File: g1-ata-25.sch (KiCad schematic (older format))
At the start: 1 part

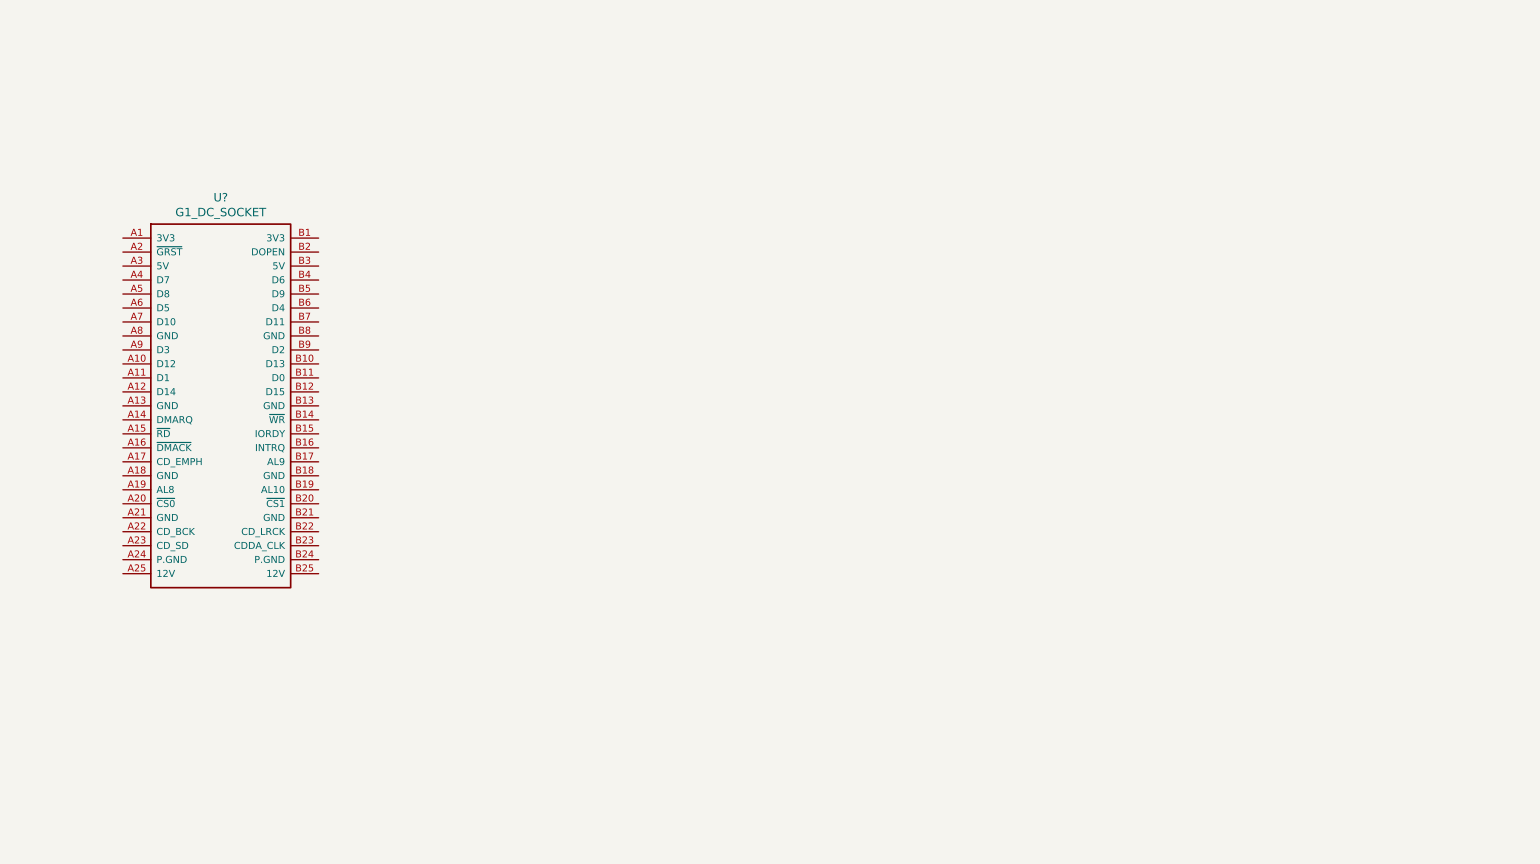
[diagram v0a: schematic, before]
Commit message: Added IDE connectors and enhanced g1-dc-socket numbering.
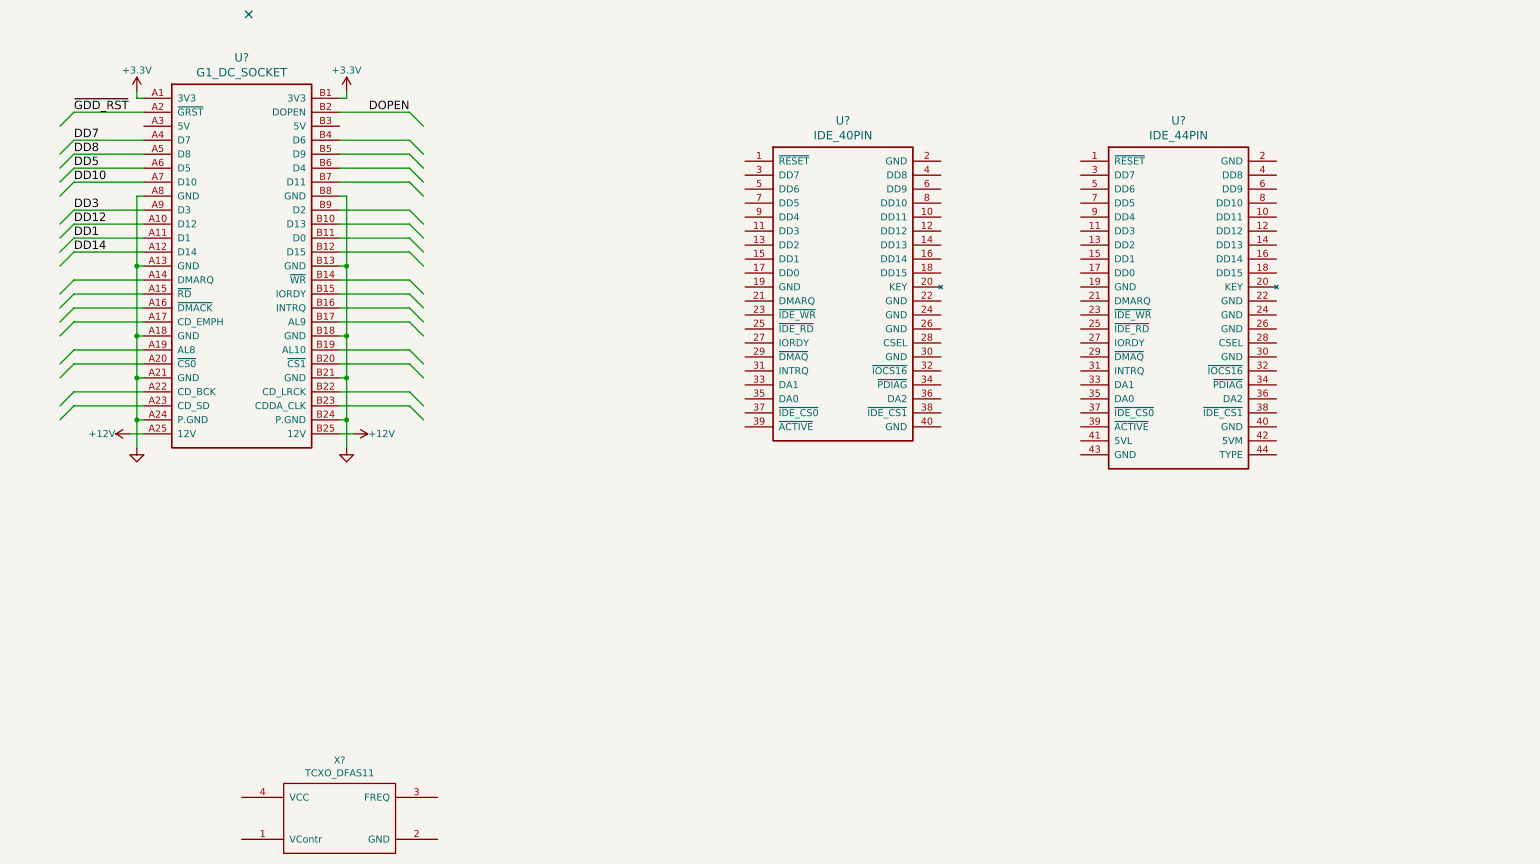
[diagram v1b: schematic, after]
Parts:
- added U?: IDE_40PIN, symbol IDE_40PIN
- added U?: IDE_44PIN, symbol IDE_44PIN
- added X?: TCXO_DFAS11, symbol TCXO_DFAS11
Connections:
- net +3V3: now reaches U?.A1 (3V3)
- net +3V3: now also U?.B1 (3V3)
- net DD12: now reaches U?.A10 (D12)
- net DD1: now reaches U?.A11 (D1)
- net DD14: now reaches U?.A12 (D14)
- net GND: now reaches U?.A13 (GND)
- net GND: now also U?.A18 (GND), U?.A21 (GND), U?.A24 (P.GND), U?.A8 (GND), U?.B13 (GND), U?.B18 (GND), U?.B21 (GND), U?.B24 (P.GND), U?.B8 (GND)
- net ~GDD_RST: now reaches U?.A2 (~GRST)
- net +12V: now reaches U?.A25 (12V)
- net +12V: now also U?.B25 (12V)
- net DD7: now reaches U?.A4 (D7)
- net DD8: now reaches U?.A5 (D8)
- net DD5: now reaches U?.A6 (D5)
- net DD10: now reaches U?.A7 (D10)
- net DD3: now reaches U?.A9 (D3)
- net DOPEN: now reaches U?.B2 (DOPEN)
- no-connect marks 0 -> 1
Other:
- moved on the sheet: U?

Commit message: Wired connectors.
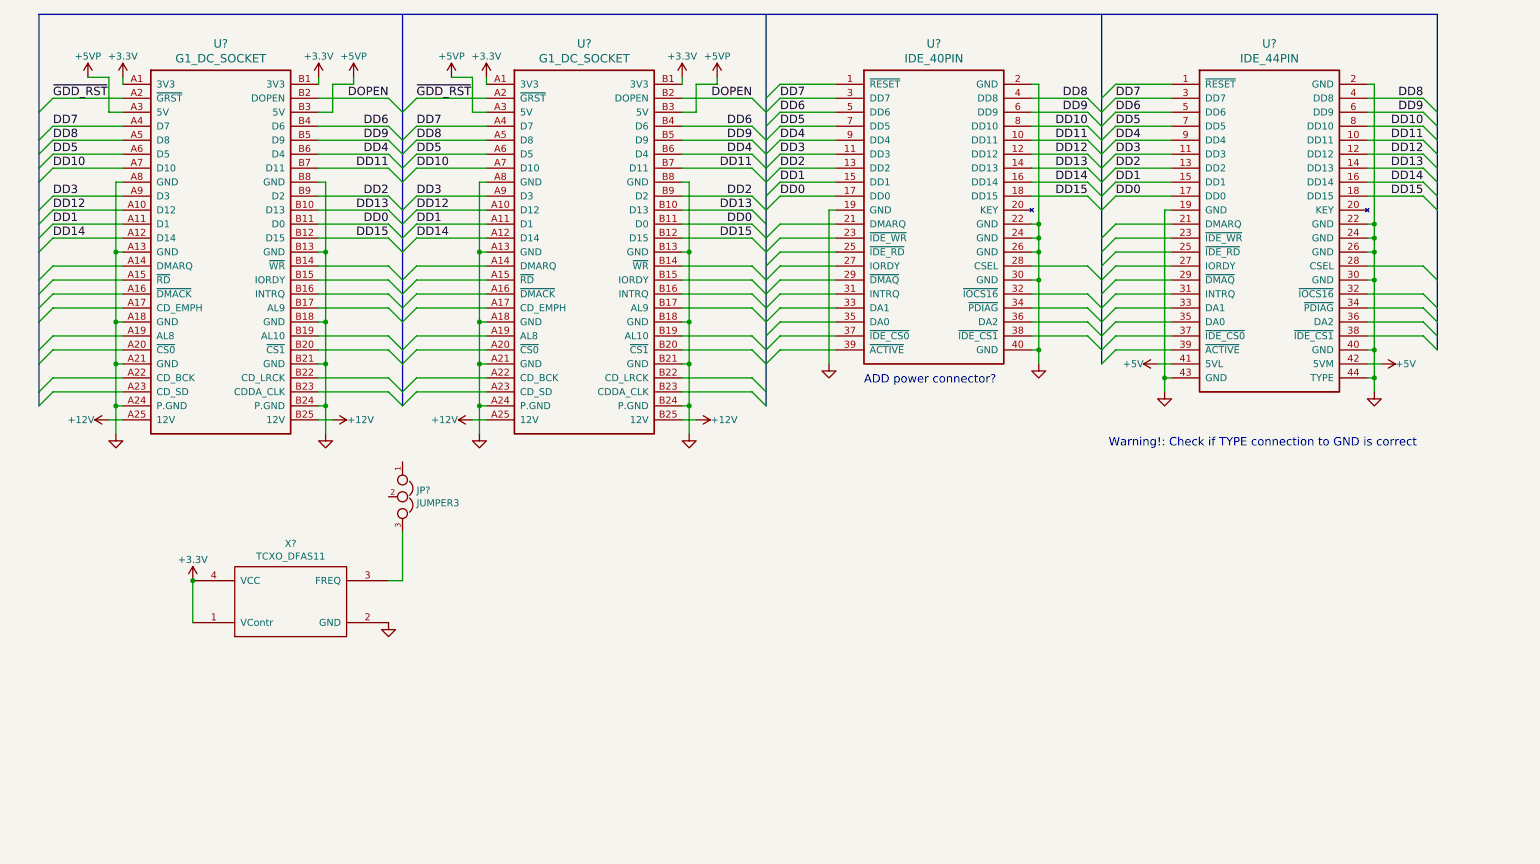
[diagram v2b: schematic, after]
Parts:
- added JP?: JUMPER3, symbol JUMPER3
- added U?: G1_DC_SOCKET, symbol G1_DC_SOCKET
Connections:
- net +12V: now also U?.A25 (12V), U?.B25 (12V)
- net +3V3: now also X?.1 (VContr), X?.4 (VCC), U?.A1 (3V3), U?.B1 (3V3)
- net DD1: now also U?.15 (DD1), U?.15 (DD1), U?.A11 (D1)
- net DD10: now also U?.8 (DD10), U?.8 (DD10), U?.A7 (D10)
- net DD12: now also U?.12 (DD12), U?.12 (DD12), U?.A10 (D12)
- net DD14: now also U?.16 (DD14), U?.16 (DD14), U?.A12 (D14)
- net DD3: now also U?.11 (DD3), U?.11 (DD3), U?.A9 (D3)
- net DD5: now also U?.7 (DD5), U?.7 (DD5), U?.A6 (D5)
- net DD7: now also U?.3 (DD7), U?.3 (DD7), U?.A4 (D7)
- net DD8: now also U?.4 (DD8), U?.4 (DD8), U?.A5 (D8)
- net DOPEN: now also U?.B2 (DOPEN)
- net GND: now also U?.19 (GND), U?.19 (GND), U?.2 (GND), U?.2 (GND), U?.22 (GND), U?.22 (GND), U?.24 (GND), U?.24 (GND), U?.26 (GND), U?.26 (GND), U?.30 (GND), U?.30 (GND), U?.40 (GND), U?.40 (GND), U?.43 (GND), U?.44 (TYPE), X?.2 (GND), U?.A13 (GND), U?.A18 (GND), U?.A21 (GND), U?.A24 (P.GND), U?.A8 (GND), U?.B13 (GND), U?.B18 (GND), U?.B21 (GND), U?.B24 (P.GND), U?.B8 (GND)
- net ~GDD_RST: now also U?.A2 (~GRST)
- net +5VP: now reaches U?.A3 (5V)
- net +5VP: now also U?.B3 (5V), U?.A3 (5V), U?.B3 (5V)
- net DD13: now reaches U?.B10 (D13)
- net DD13: now also U?.14 (DD13), U?.14 (DD13), U?.B10 (D13)
- net DD0: now reaches U?.B11 (D0)
- net DD0: now also U?.17 (DD0), U?.17 (DD0), U?.B11 (D0)
- net DD15: now reaches U?.B12 (D15)
- net DD15: now also U?.18 (DD15), U?.18 (DD15), U?.B12 (D15)
- net DD6: now reaches U?.B4 (D6)
- net DD6: now also U?.5 (DD6), U?.5 (DD6), U?.B4 (D6)
- net DD9: now reaches U?.B5 (D9)
- net DD9: now also U?.6 (DD9), U?.6 (DD9), U?.B5 (D9)
- net DD4: now reaches U?.B6 (D4)
- net DD4: now also U?.9 (DD4), U?.9 (DD4), U?.B6 (D4)
- net DD11: now reaches U?.B7 (D11)
- net DD11: now also U?.10 (DD11), U?.10 (DD11), U?.B7 (D11)
- net DD2: now reaches U?.B9 (D2)
- net DD2: now also U?.13 (DD2), U?.13 (DD2), U?.B9 (D2)
- net at X?.3 (FREQ): now also JP?.3
- net +5V: now reaches U?.41 (5VL)
- net +5V: now also U?.42 (5VM)
- no-connect marks 1 -> 0
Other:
- note added: "ADD power connector?"
- note added: "Warning!: Check if TYPE connection to GND is correct"
- moved on the sheet: U?, X?

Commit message: Added LED and connectors, wired some more elements.
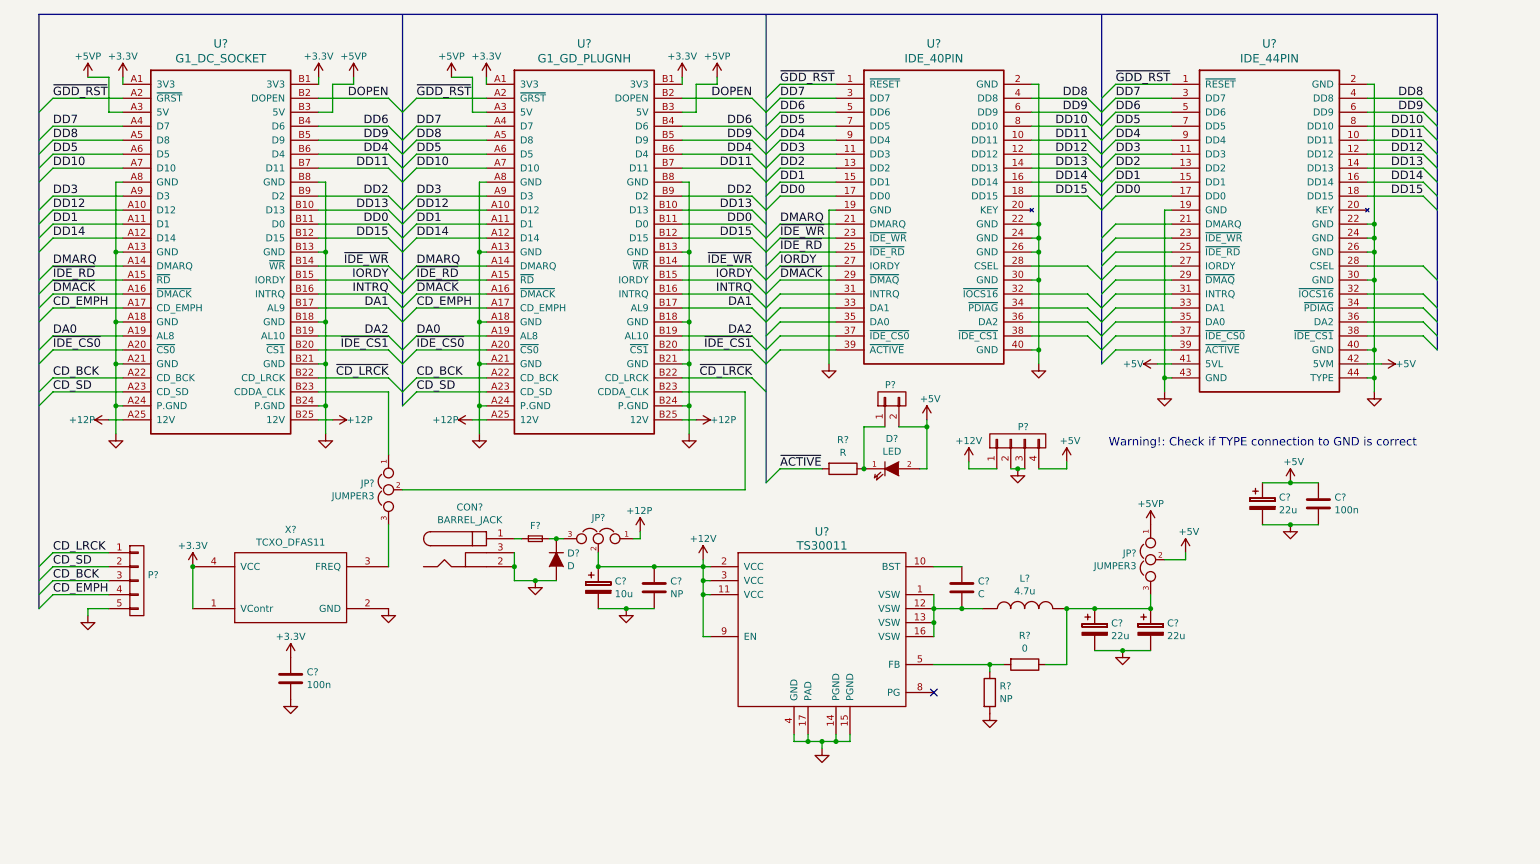
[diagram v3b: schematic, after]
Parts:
- added C?: C, symbol C
- added C? (x3): 22u, symbol CP
- added C?: 10u, symbol CP
- added C?: NP, symbol C
- added C? (x2): 100n, symbol C
- added CON?: BARREL_JACK, symbol BARREL_JACK
- added D?: D, symbol D
- added D?: LED, symbol LED
- added F?: F_Small, symbol F_Small
- added JP? (x2): JUMPER3, symbol JUMPER3
- added L?: 4.7u, symbol INDUCTOR
- added P?: CONN_01X02, symbol CONN_01X02
- added P?: CONN_01X05, symbol CONN_01X05
- added P?: CONN_01X04, symbol CONN_01X04
- added R?: NP, symbol R
- added R?: 0, symbol R
- added R?: R, symbol R
- added U?: TS30011, symbol TS30011
- U?: value G1_DC_SOCKET -> G1_GD_PLUGNH
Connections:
- net +12V: now also C?.1, C?.1, JP?.2, P?.1 (P1), U?.11 (VCC), U?.2 (VCC), U?.3 (VCC), U?.9 (EN); no longer U?.A25 (12V), U?.A25 (12V), U?.B25 (12V), U?.B25 (12V)
- net +3V3: now also C?.1
- net +5V: now also C?.1, C?.1, D?.2 (A), JP?.2, P?.2 (P2), P?.4 (P4)
- net +5VP: now also JP?.1
- net GND: now also C?.2, C?.2, C?.2, C?.2, C?.2, C?.2, C?.2, CON?.2, CON?.3, D?.2 (A), P?.2 (P2), P?.3 (P3), P?.5 (P5), R?.2, U?.14 (PGND), U?.15 (PGND), U?.17 (PAD), U?.4 (GND)
- net ~GDD_RST: now also U?.1 (~RESET), U?.1 (~RESET)
- net DMARQ: now reaches U?.A14 (DMARQ)
- net DMARQ: now also U?.21 (DMARQ), U?.A14 (DMARQ)
- net ~IDE_RD: now reaches U?.A15 (~RD)
- net ~IDE_RD: now also U?.25 (~IDE_RD), U?.A15 (~RD)
- net ~DMACK: now reaches U?.A16 (~DMACK)
- net ~DMACK: now also U?.29 (~DMAQ), U?.A16 (~DMACK)
- net CD_EMPH: now reaches U?.A17 (CD_EMPH)
- net CD_EMPH: now also U?.A17 (CD_EMPH), P?.4 (P4)
- net DA0: now reaches U?.A19 (AL8)
- net DA0: now also U?.A19 (AL8)
- net ~IDE_CS0: now reaches U?.A20 (~CS0)
- net ~IDE_CS0: now also U?.A20 (~CS0)
- net CD_BCK: now reaches U?.A22 (CD_BCK)
- net CD_BCK: now also U?.A22 (CD_BCK), P?.3 (P3)
- net CD_SD: now reaches U?.A23 (CD_SD)
- net CD_SD: now also U?.A23 (CD_SD), P?.2 (P2)
- net ~IDE_WR: now reaches U?.B14 (~WR)
- net ~IDE_WR: now also U?.23 (~IDE_WR), U?.B14 (~WR)
- net IORDY: now reaches U?.B15 (IORDY)
- net IORDY: now also U?.27 (IORDY), U?.B15 (IORDY)
- net INTRQ: now reaches U?.B16 (INTRQ)
- net INTRQ: now also U?.B16 (INTRQ)
- net DA1: now reaches U?.B17 (AL9)
- net DA1: now also U?.B17 (AL9)
- net DA2: now reaches U?.B19 (AL10)
- net DA2: now also U?.B19 (AL10)
- net ~IDE_CS1: now reaches U?.B20 (~CS1)
- net ~IDE_CS1: now also U?.B20 (~CS1)
- net ~CD_LRCK: now reaches U?.B22 (CD_LRCK)
- net ~CD_LRCK: now also U?.B22 (CD_LRCK)
- net at U?.B23 (CDDA_CLK): now also JP?.1
- net at U?.B23 (CDDA_CLK): now also JP?.2
- new net: C?.2, L?.1, U?.1 (VSW), U?.12 (VSW), U?.13 (VSW), U?.16 (VSW)
- new net: C?.1, U?.10 (BST)
- new net: R?.1, R?.2, U?.5 (FB)
- new net: C?.1, C?.1, JP?.3, L?.2, R?.1
- new net: D?.1 (K), F?.2, JP?.3
- new net: CON?.1, F?.1
- new net: D?.1 (K), P?.1 (P1), R?.1
- new net +12P: JP?.1, U?.A25 (12V), U?.A25 (12V), U?.B25 (12V), U?.B25 (12V)
- new net CD_LRCK: P?.1 (P1)
- new net ~ACTIVE: R?.2
- no-connect marks 0 -> 1
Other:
- note removed: "ADD power connector?"
- moved on the sheet: JP?, X?

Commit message: Schematic almost finished (just needs a revision).
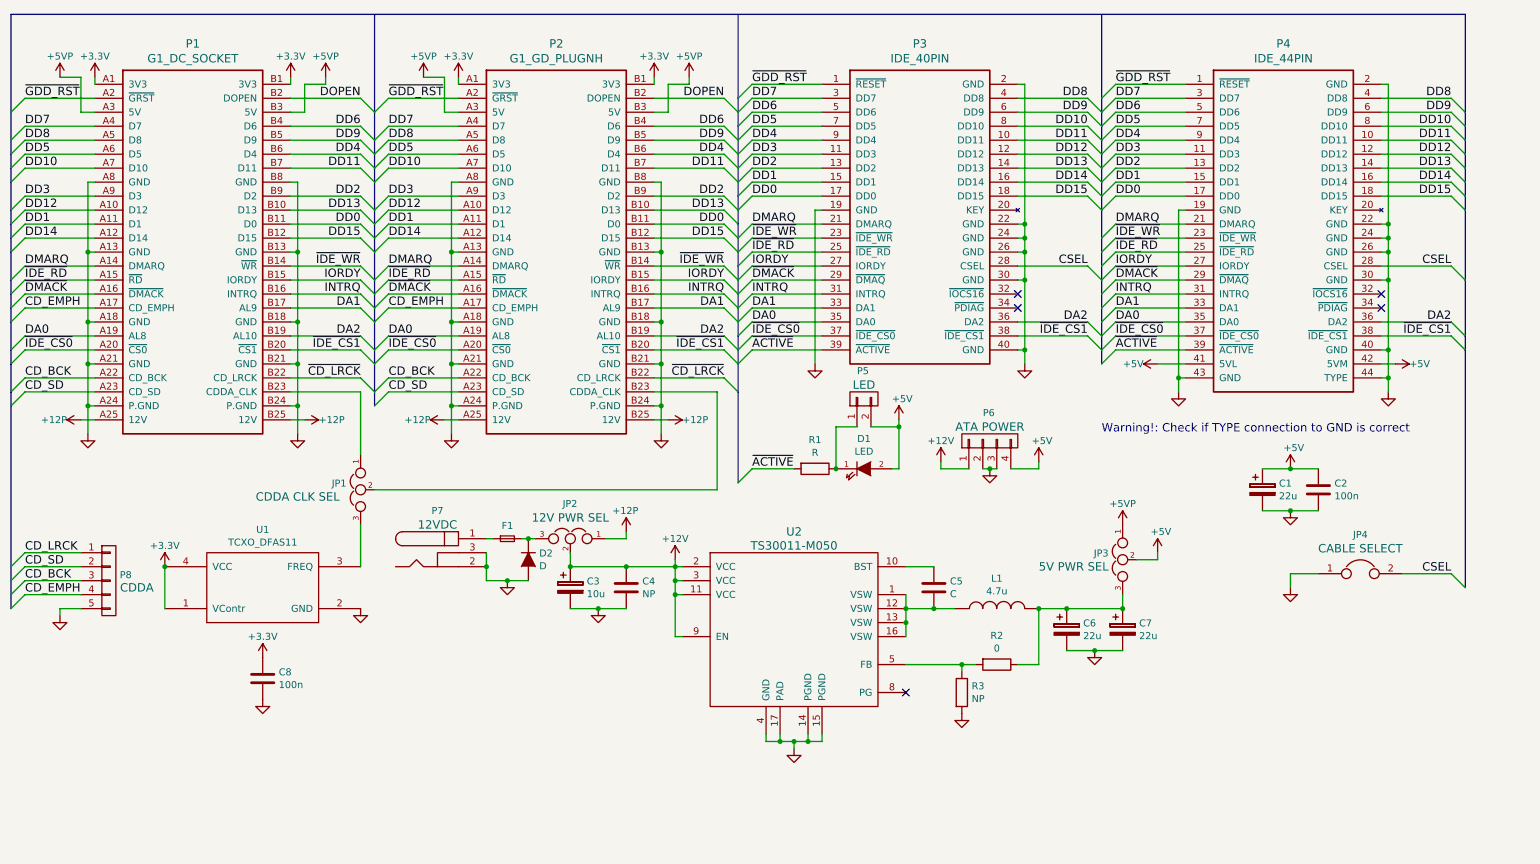
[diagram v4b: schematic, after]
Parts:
- added JP4: JUMPER, symbol JUMPER
- JP1: renamed from JP?; Func (none) -> CDDA CLK SEL
- JP2: renamed from JP?; Func (none) -> 12V PWR SEL
- JP3: renamed from JP?; Func (none) -> 5V PWR SEL
- P5: renamed from P?; Func (none) -> LED
- P6: renamed from P?; Func (none) -> ATA POWER
- P7: renamed from CON?; Func (none) -> 12VDC
- P8: renamed from P?; Func (none) -> CDDA
- U2: renamed from U?; value TS30011 -> TS30011-M050; manf# (none) -> TS30011-M050QFNR
- gave numbers to parts that had none: 20
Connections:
- net DA0: now also P3.35 (DA0), P4.35 (DA0)
- net DA1: now also P3.33 (DA1), P4.33 (DA1)
- net DA2: now also P3.36 (DA2), P4.36 (DA2)
- net DMARQ: now also P4.21 (DMARQ)
- net GND: now also JP4.1
- net INTRQ: now also P3.31 (INTRQ), P4.31 (INTRQ)
- net IORDY: now also P4.27 (IORDY)
- net ~ACTIVE: now also P3.39 (~ACTIVE), P4.39 (~ACTIVE)
- net ~DMACK: now also P4.29 (~DMAQ)
- net ~IDE_CS0: now also P3.37 (~IDE_CS0), P4.37 (~IDE_CS0)
- net ~IDE_CS1: now also P3.38 (~IDE_CS1), P4.38 (~IDE_CS1)
- net ~IDE_RD: now also P4.25 (~IDE_RD)
- net ~IDE_WR: now also P4.23 (~IDE_WR)
- net CSEL: now reaches P3.28 (CSEL)
- net CSEL: now also P4.28 (CSEL), JP4.2
- no-connect marks 1 -> 5
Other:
- moved on the sheet: C1, C2, C3, C4, C5, C6, C7, C8, D1, D2, F1, JP1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

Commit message: First test placing components.
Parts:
- C1, C6, C7, L1: footprint (none) -> Capacitors_SMD:C_1206
- C2, C3, C4, C5, C8, F1: footprint (none) -> Capacitors_SMD:C_0805
- D1: footprint (none) -> LEDs:LED_0603
- D2: footprint (none) -> Diodes_SMD:MiniMELF_Standard
- JP1, JP2, JP3: footprint (none) -> Pin_Headers:Pin_Header_Straight_1x03
- JP4: footprint (none) -> Pin_Headers:Pin_Header_Straight_1x02
- P1: footprint (none) -> doragasu:MOLEX_53408-0570
- P2: footprint (none) -> doragasu:MOLEX_52584-0508
- P3: footprint (none) -> Socket_Strips:Socket_Strip_Straight_2x20
- P4: footprint (none) -> doragasu:SOCKET_2X22_2MM_ANGLE
- P5: footprint (none) -> Socket_Strips:Socket_Strip_Straight_1x02
- P6: footprint (none) -> Socket_Strips:Socket_Strip_Straight_1x04
- P7: footprint (none) -> Connect:BARREL_JACK
- P8: footprint (none) -> Socket_Strips:Socket_Strip_Straight_1x05
- R1, R2, R3: footprint (none) -> Resistors_SMD:R_0805
- U1: footprint (none) -> doragasu:OSC_F530L
- U2: footprint (none) -> Housings_DFN_QFN:QFN-16-1EP_3x3mm_Pitch0.5mm

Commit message: Moved some components.
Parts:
- P3: footprint Socket_Strips:Socket_Strip_Straight_2x20 -> Pin_Headers:Pin_Header_Straight_2x20
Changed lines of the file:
@@
 F 0 "P3" H 7150 1640 60  0000 C CNN
 F 1 "IDE_40PIN" H 7150 1534 60  0000 C CNN
-F 2 "Socket_Strips:Socket_Strip_Straight_2x20" H 6450 1350 60  0001 C CNN
+F 2 "Pin_Headers:Pin_Header_Straight_2x20" H 6450 1350 60  0001 C CNN
 F 3 "" H 6450 1350 60  0000 C CNN
 	1    6450 1350
